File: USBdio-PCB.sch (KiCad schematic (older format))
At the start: 68 parts, among them IC1 ATMEGA328-P, P0 RELAY_(JSM1A-12V-4), P1 RELAY_(JSM1A-12V-4), P2 RELAY_(JSM1A-12V-4), P3 RELAY_(JSM1A-12V-4), P4 RELAY_(JSM1A-12V-4), P5 RELAY_(JSM1A-12V-4), P6 RELAY_(JSM1A-12V-4), P7 RELAY_(JSM1A-12V-4), P8 CONN_01X03, Q1 Q_NPN_BEC, Q10 Q_NPN, Q11 Q_NPN, Q12 Q_NPN, Q13 Q_NPN, Q14 Q_NPN, Q15 Q_NPN, Q16 Q_NPN, Q17 Q_NPN, Q2 Q_NPN_BEC, Q3 Q_NPN_BEC, Q4 Q_NPN_BEC, Q5 Q_NPN_BEC, Q6 Q_NPN_BEC, Q7 Q_NPN_BEC, Q8 Q_NPN_BEC, Q9 Q_NPN_BEC, U1 NCV7805BDTRKG, X1 CRYSTAL_SMD

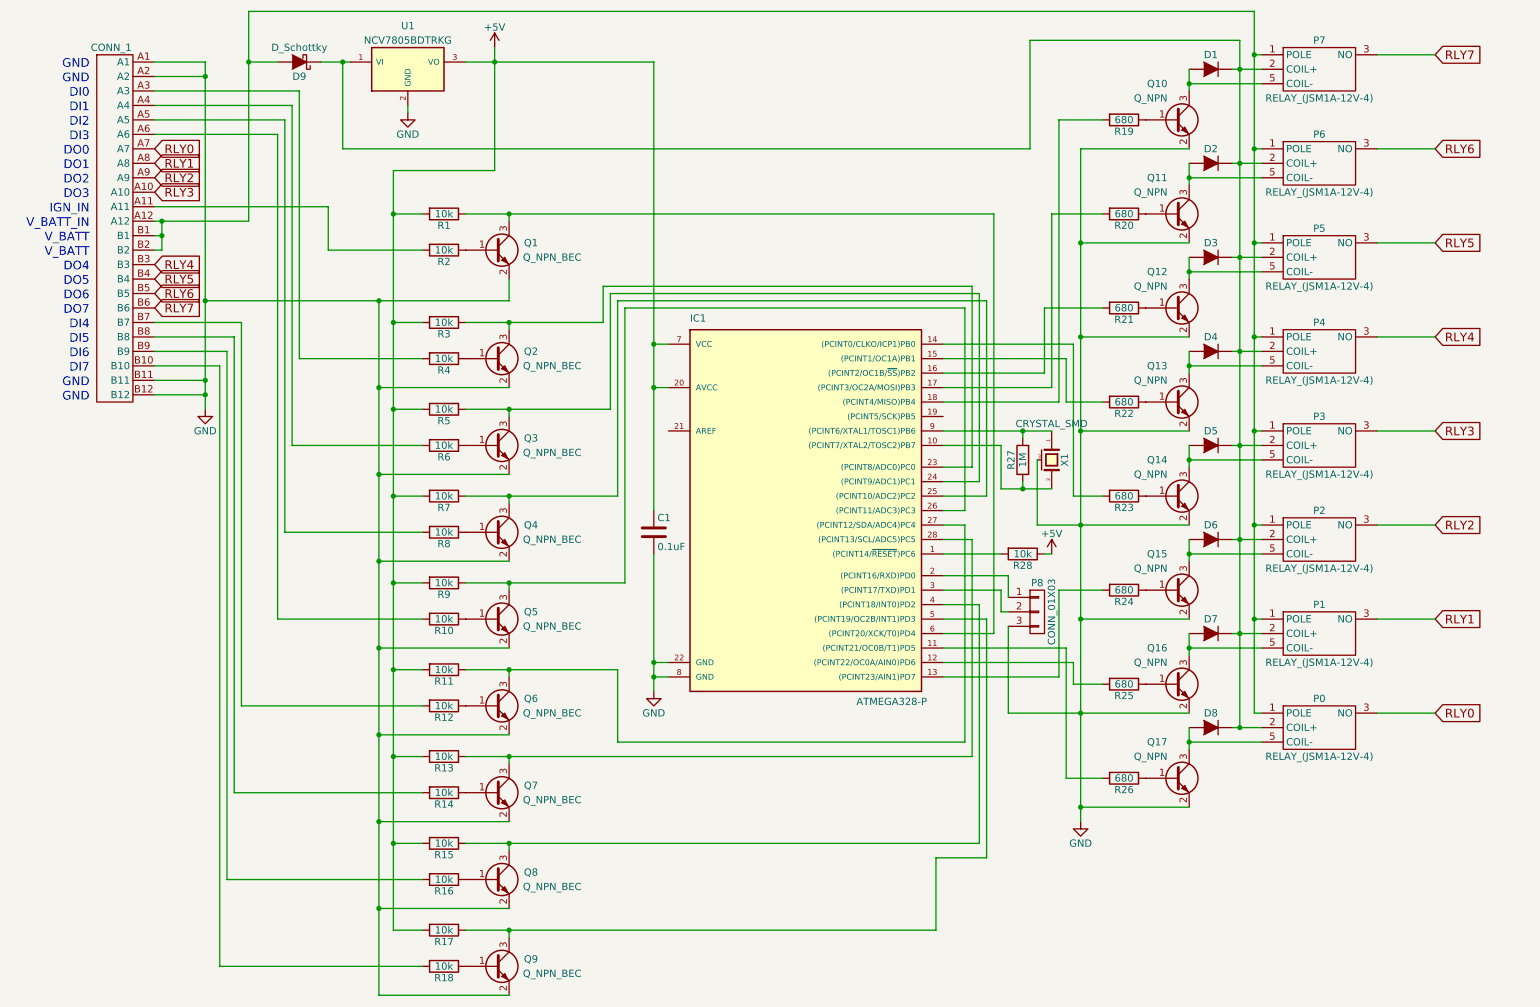
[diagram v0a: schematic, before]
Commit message: Reduced to 6 in 6 out, and added COM lines to connector.
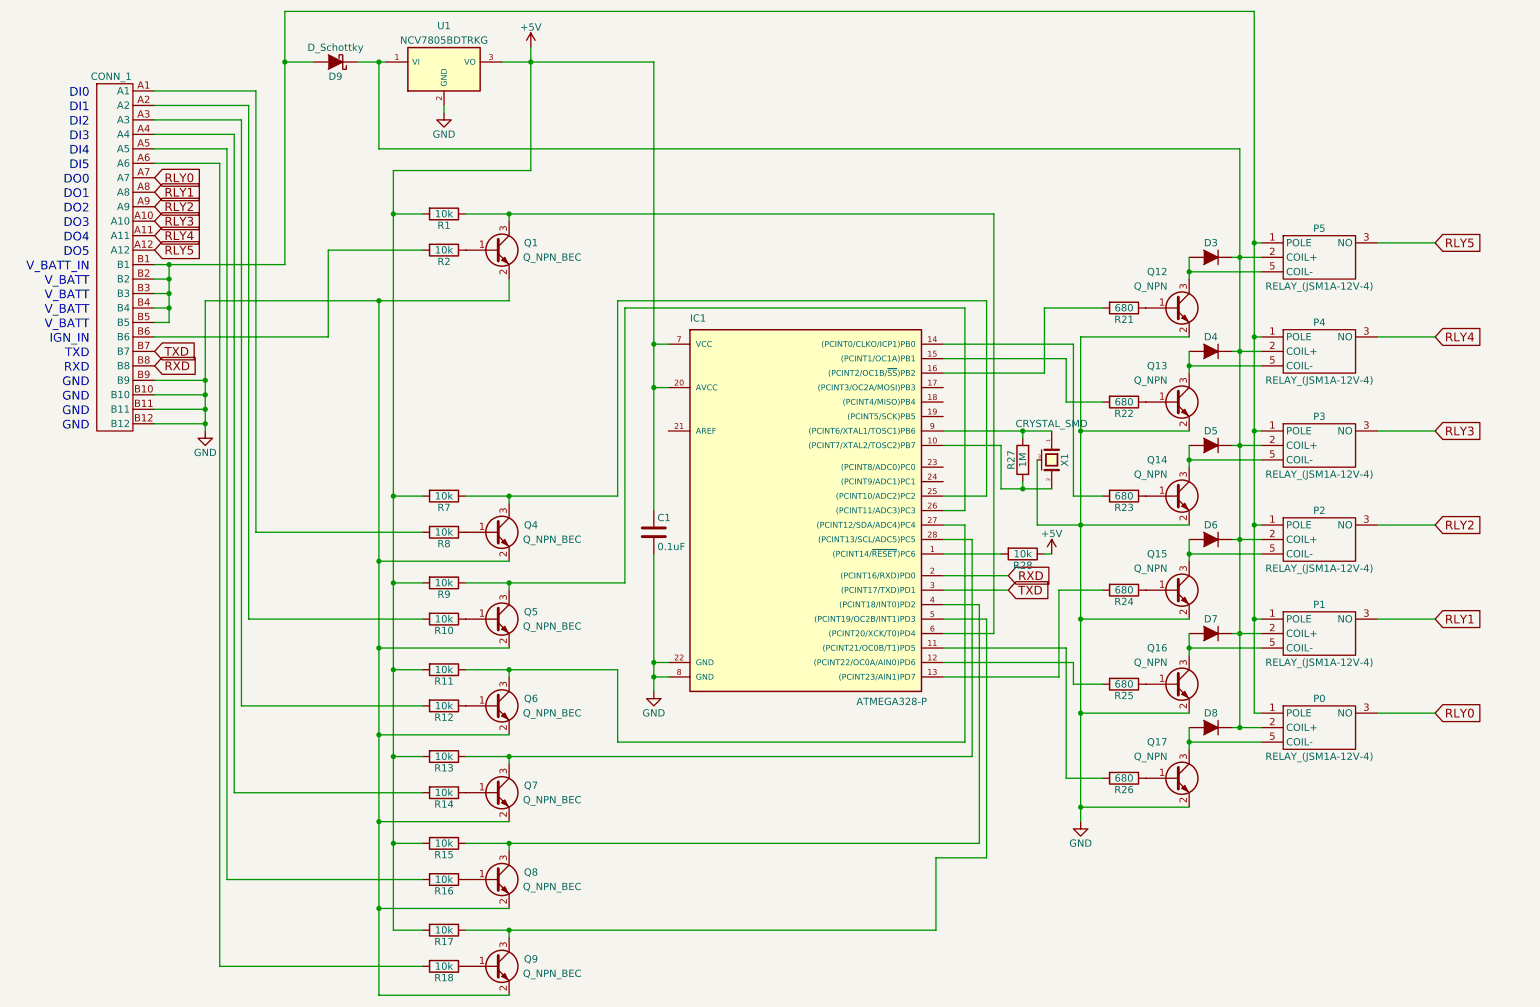
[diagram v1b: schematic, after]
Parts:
- removed D1, D2: D, Resistors_SMD:R_1206_HandSoldering, symbol D
- removed P6, P7: RELAY_(JSM1A-12V-4), symbol RELAY_(JSM1A-12V-4)
- removed P8: CONN_01X03, Pin_Headers:Pin_Header_Straight_1x03, symbol CONN_01X03
- removed Q10, Q11: Q_NPN, TO_SOT_Packages_SMD:SOT-23_Handsoldering, symbol Q_NPN_BEC
- removed Q2, Q3: Q_NPN_BEC, TO_SOT_Packages_SMD:SOT-23_Handsoldering, symbol Q_NPN_BEC
- removed R19, R20: 680, Resistors_SMD:R_1206_HandSoldering, symbol R
- removed R3, R4, R5, R6: 10k, Resistors_SMD:R_1206_HandSoldering, symbol R
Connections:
- net RLY6 is gone; now on an unnamed net: CONN_1.B5
- net RLY7 is gone; now on an unnamed net: CONN_1.B6
- net GND: now also CONN_1.B10, CONN_1.B9; no longer CONN_1.A1, CONN_1.A2
- net RLY4: now also CONN_1.A11; no longer CONN_1.B3
- net RLY5: now also CONN_1.A12; no longer CONN_1.B4
- net at CONN_1.A3: now also R12.2
- net at CONN_1.A4: now also R14.2
- net at R8.2: now also CONN_1.A1; no longer CONN_1.A5
- net at R10.2: now also CONN_1.A2; no longer CONN_1.A6
- net TXD: now reaches CONN_1.B7
- net TXD: now also IC1.3 ((PCINT17/TXD)PD1); no longer R12.2
- net RXD: now reaches CONN_1.B8
- net RXD: now also IC1.2 ((PCINT16/RXD)PD0); no longer R14.2
- net at R16.2: now also CONN_1.A5; no longer CONN_1.B9
- net at R18.2: now also CONN_1.A6; no longer CONN_1.B10
- net at R2.2: no longer CONN_1.A11
- net at CONN_1.B1, CONN_1.B2, D9.2 (A)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: now also CONN_1.B3, CONN_1.B4; no longer CONN_1.A12
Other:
- note added: "RXD"
- note added: "TXD"
- note removed: "DI6"
- note removed: "DI7"
- note removed: "DO6"
- note removed: "DO7"
- moved on the sheet: CONN_1, D9, U1

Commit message: -added CH340G and a self-resetting fuse -corrected errors from v1.1
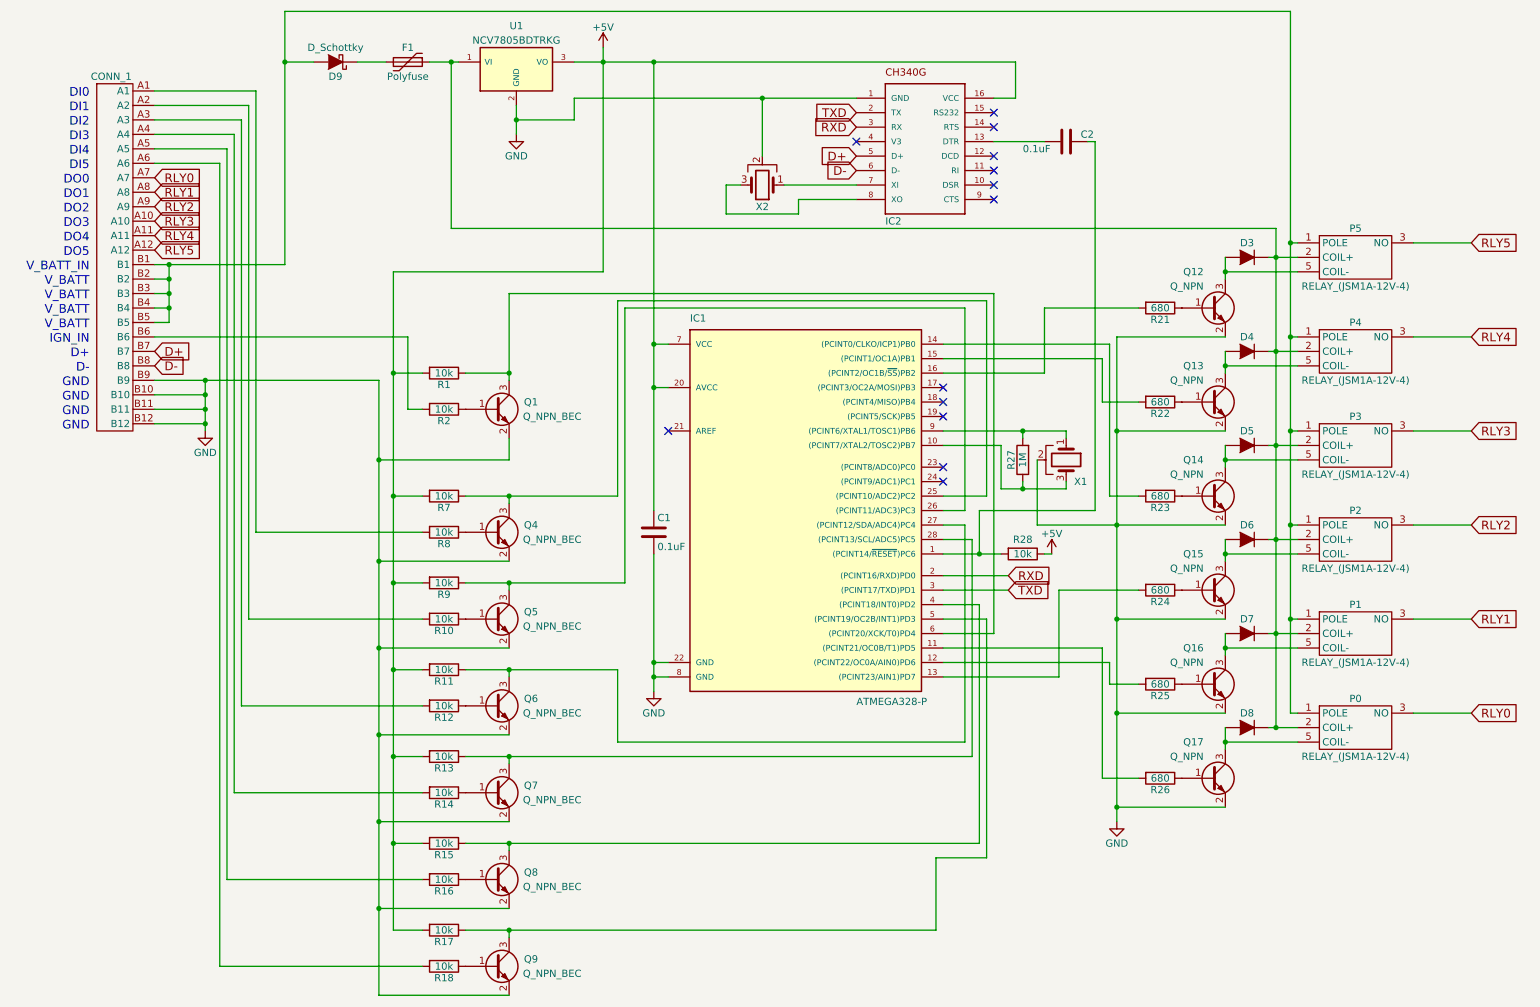
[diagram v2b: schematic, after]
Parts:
- removed X1: CRYSTAL_SMD, USBdio-PCB:RESONATOR_(CSTCE16M0V53C-R0), symbol CRYSTAL_SMD
- added C2: 0.1uF, USBdio-PCB:R_1206_HandSoldering_(narrow), symbol C
- added F1: Polyfuse, Resistors_SMD:R_1812_HandSoldering, symbol Polyfuse
- added IC2: CH340G, USBdio-PCB:CH340G, symbol CH340G
- added X1, X2: Crystal_GND2, USBdio-PCB:RESONATOR_(CSTCE16M0V53C-R0), symbol Crystal_GND2
- C1: footprint (none) -> USBdio-PCB:R_1206_HandSoldering_(narrow)
- D3, D4, D5, D6, D7, D8, R1, R10, R11, R12, R13, R14, R15, R16, R17, R18, R2, R21, R22, R23, R24, R25, R26, R27, R28, R7, R8, R9: footprint Resistors_SMD:R_1206_HandSoldering -> USBdio-PCB:R_1206_HandSoldering_(narrow)
- P0, P1, P2, P3, P4, P5: footprint (none) -> USBdio-PCB:RELAY_(JSM1A-12V-4)
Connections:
- net +5V: now also IC2.16 (VCC)
- net GND: now also IC2.1 (GND), X1.2, X2.2
- net RXD: now also IC2.3 (RX); no longer CONN_1.B8
- net TXD: now also IC2.2 (TX); no longer CONN_1.B7
- net at D3.1 (K), D4.1 (K), D5.1 (K)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: now also F1.1; no longer D9.1 (K)
- net at IC1.1 ((PCINT14/~RESET~)PC6), R28.2: now also C2.1
- net at IC1.10 ((PCINT7/XTAL2/TOSC2)PB7), R27.1: now also X1.3
- net at IC1.9 ((PCINT6/XTAL1/TOSC1)PB6), R27.2: now also X1.1
- new net: D9.1 (K), F1.2
- new net: C2.2, IC2.13 (DTR)
- new net: IC2.7 (XI), X2.1
- new net: IC2.8 (XO), X2.3
- new net D+: CONN_1.B7, IC2.5 (D+)
- new net D-: CONN_1.B8, IC2.6 (D-)
- no-connect marks 0 -> 13
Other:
- note added: "D+"
- note added: "D-"
- note removed: "RXD"
- note removed: "TXD"
- moved on the sheet: D3, D4, D5, D6, D7, D8, P0, P1, P2, P3, P4, P5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

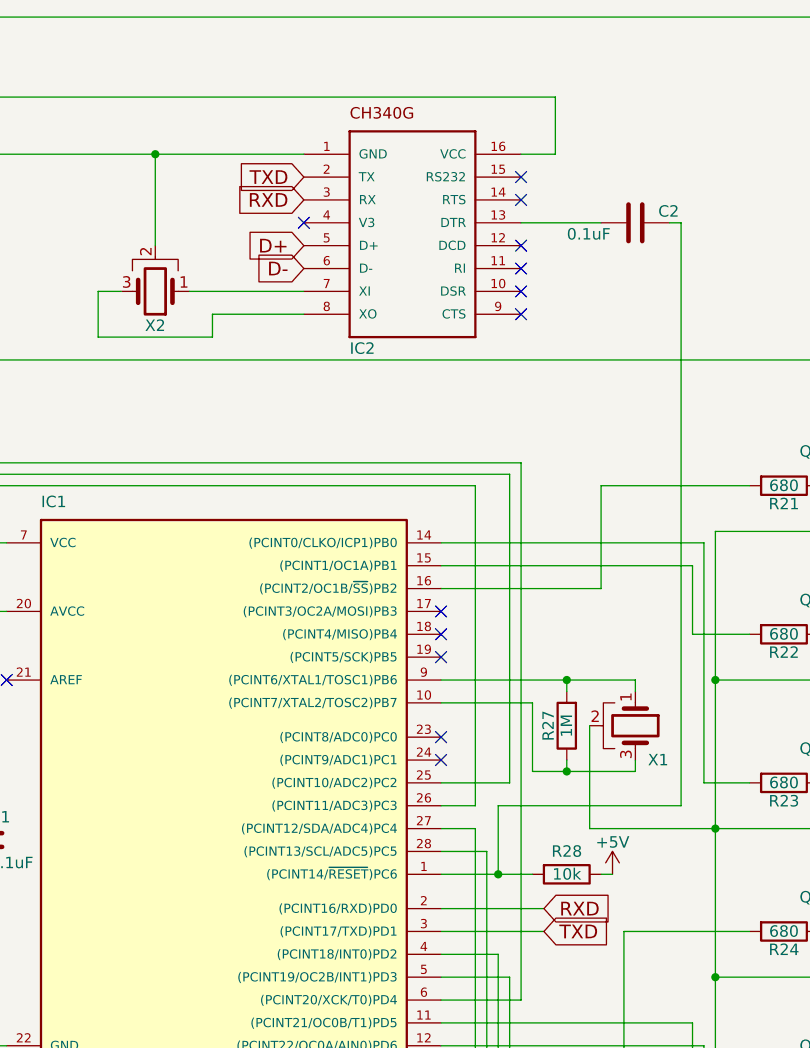
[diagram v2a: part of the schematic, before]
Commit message: -Switched Tx and Rx. -Changed reset pull-up from 10kohm to 1kohm.
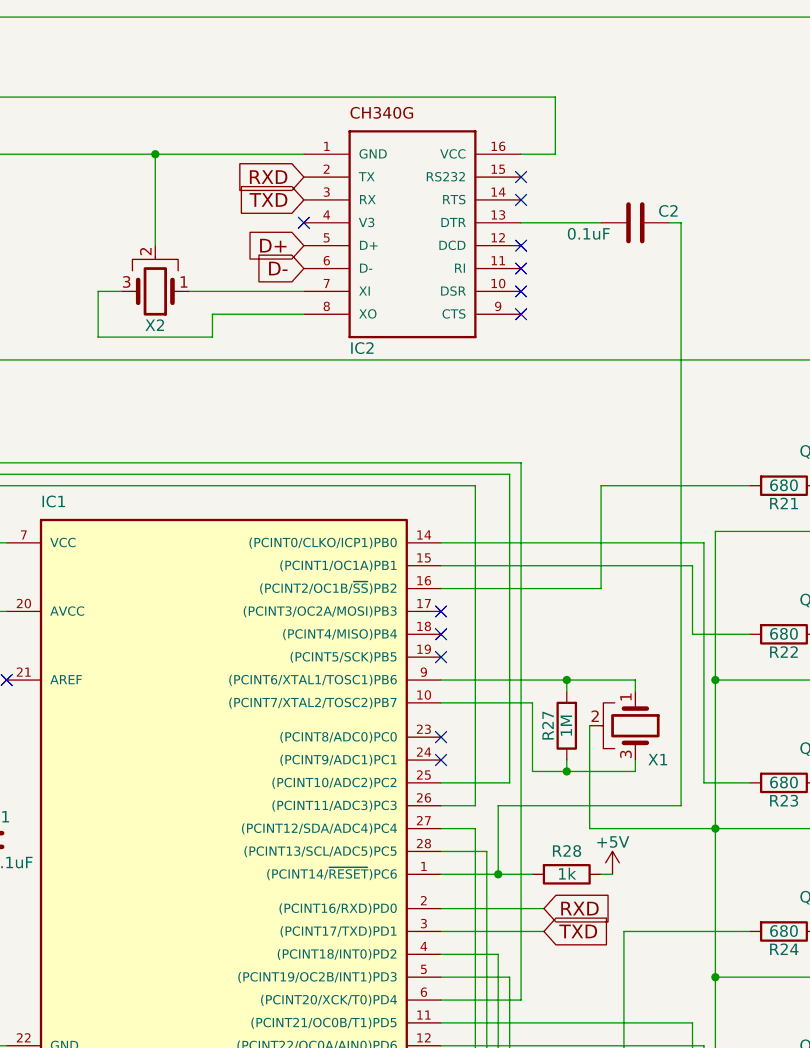
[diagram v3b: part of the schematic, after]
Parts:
- R28: value 10k -> 1k
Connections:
- net RXD: now also IC2.2 (TX); no longer IC2.3 (RX)
- net TXD: now also IC2.3 (RX); no longer IC2.2 (TX)
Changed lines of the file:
@@
 LIBS:arduino
 LIBS:USBdio-PCB
-LIBS:CH340G
-LIBS:rpi-shutdown-pcb-cache
 LIBS:USBdio-PCB-cache
 EELAYER 25 0
@@
 P 7450 4350
 F 0 "R28" V 7350 4350 50  0000 C CNN
-F 1 "10k" V 7450 4350 50  0000 C CNN
+F 1 "1k" V 7450 4350 50  0000 C CNN
 F 2 "USBdio-PCB:R_1206_HandSoldering_(narrow)" V 7380 4350 50  0001 C CNN
 F 3 "" H 7450 4350 50  0000 C CNN
@@
 Wire Wire Line
 	5900 1900 6300 1900
+Text GLabel 6300 1400 0    60   Input ~ 0
+TXD
 Text GLabel 6300 1300 0    60   Input ~ 0
-TXD
-Text GLabel 6300 1400 0    60   Input ~ 0
 RXD
 Text GLabel 6300 1600 0    60   Input ~ 0
